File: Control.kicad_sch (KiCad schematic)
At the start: 42 parts, among them U2 LT6108IMS8-1-TRPBF, U3 LM139ADRG4, U5 LT6108IMS8-1-TRPBF

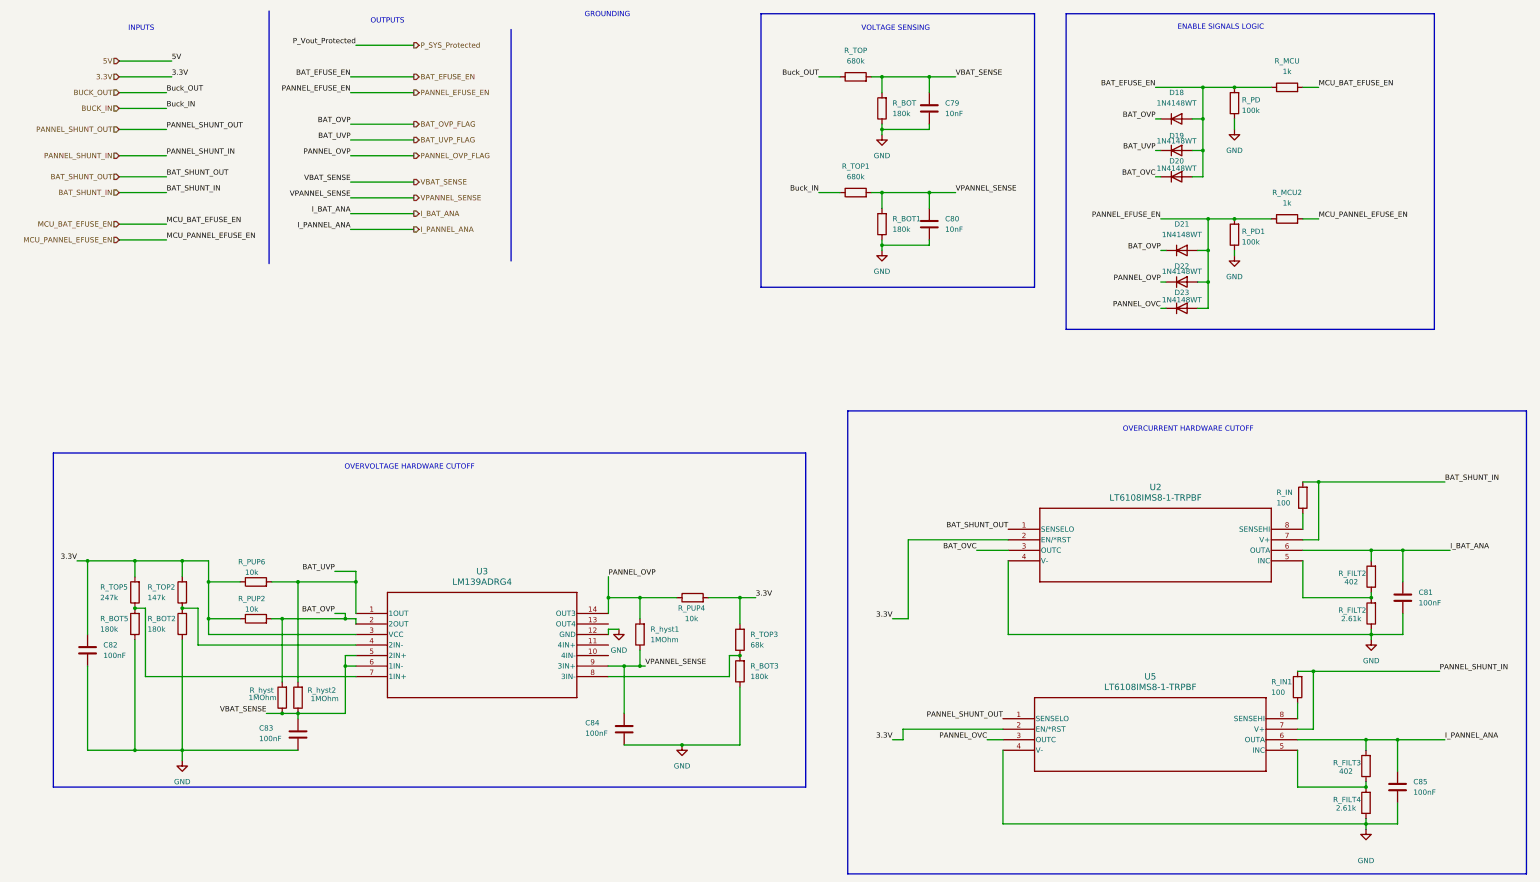
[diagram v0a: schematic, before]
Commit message: Adjusting footprints of components
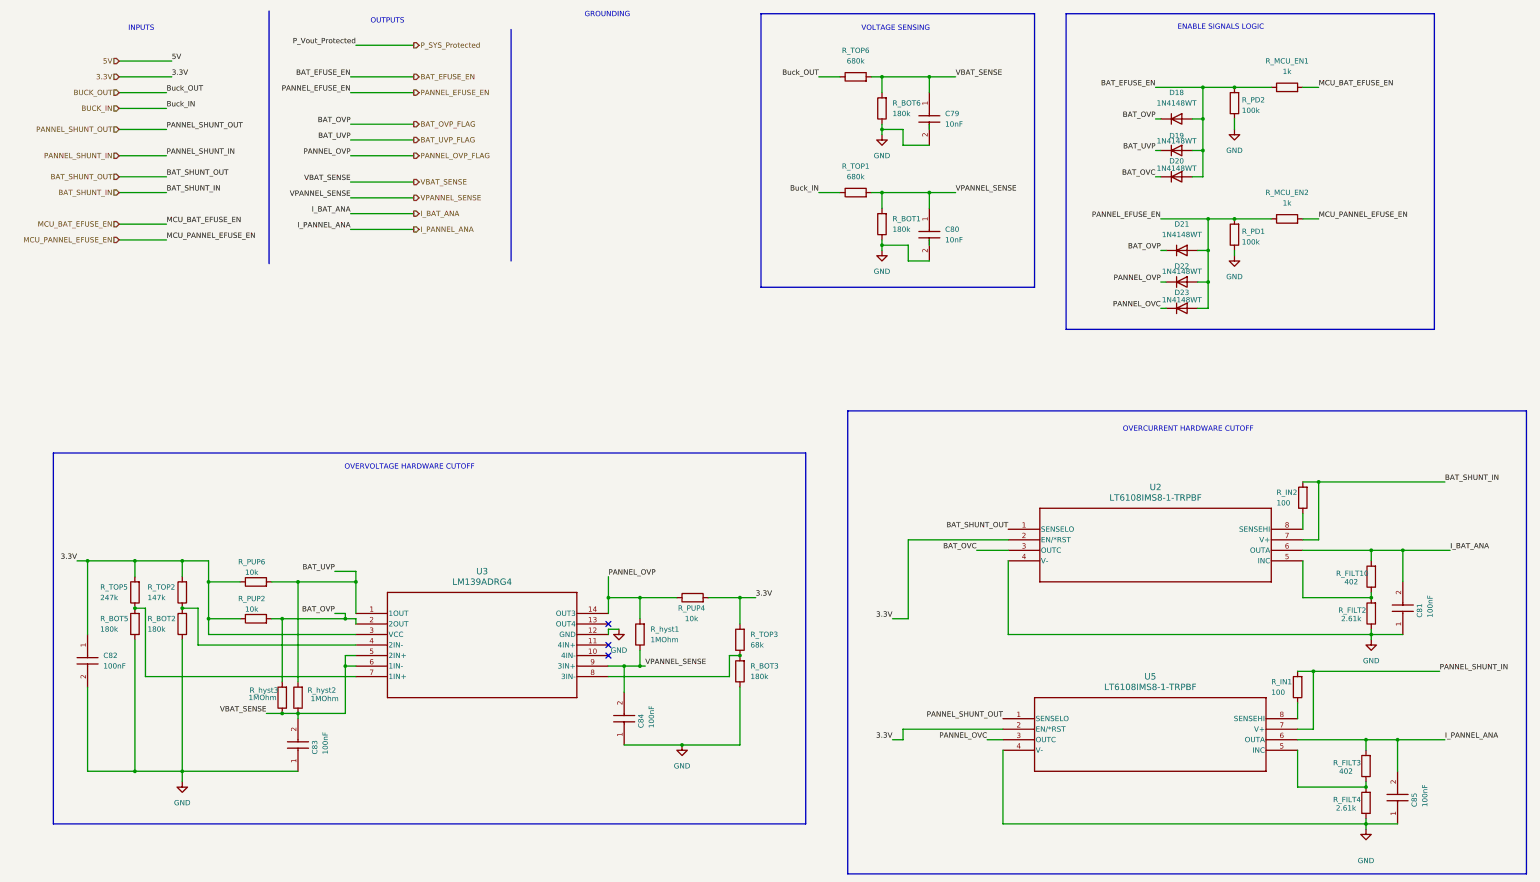
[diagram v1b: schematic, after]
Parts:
- removed C81, C84, C85: 100nF, symbol Device:C
- added C81, C84, C85: 100nF, C0603_Commercial, symbol PULSE_Library:C0603X6S0J104M030BC
- C79, C80: footprint (none) -> CAPC2012X145N; symbol Device:C -> PULSE_Library:C2012X7R1A106M125AC; Height (none) -> 1.45; Manufacturer_Name (none) -> TDK; Manufacturer_Part_Number (none) -> C2012X7R1A106M125AC; Mouser Part Number (none) -> 810-C2012X7R1A106M; Mouser Price/Stock (none) -> https://www.mouser.co.uk/ProductDetail/TDK/C2012X7R1A106M12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
- C82, C83: footprint (none) -> C0603_Commercial; symbol Device:C -> PULSE_Library:C0603X6S0J104M030BC; Height (none) -> 0.33; Manufacturer_Name (none) -> TDK; Manufacturer_Part_Number (none) -> C0603X6S0J104M030BC; Mouser Part Number (none) -> 810-C0603X6S0J104M; Mouser Price/Stock (none) -> https://www.mouser.co.uk/ProductDetail/TDK/C0603X6S0J104M03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
- R_BOT1, R_BOT2, R_BOT3, R_BOT5, R_FILT2, R_FILT3, R_FILT4, R_IN1, R_PD1, R_PUP2, R_PUP4, R_PUP6, R_TOP1, R_TOP2, R_TOP3, R_TOP5, R_hyst1, R_hyst2: footprint (none) -> Resistor_SMD:R_0603_1608Metric
- R_BOT6: renamed from R_BOT; footprint (none) -> Resistor_SMD:R_0603_1608Metric
- R_FILT10: renamed from R_FILT2; footprint (none) -> Resistor_SMD:R_0603_1608Metric
- R_IN2: renamed from R_IN; footprint (none) -> Resistor_SMD:R_0603_1608Metric
- R_MCU_EN1: renamed from R_MCU; footprint (none) -> Resistor_SMD:R_0603_1608Metric
- R_MCU_EN2: renamed from R_MCU2; footprint (none) -> Resistor_SMD:R_0603_1608Metric
- R_PD2: renamed from R_PD; footprint (none) -> Resistor_SMD:R_0603_1608Metric
- R_TOP6: renamed from R_TOP; footprint (none) -> Resistor_SMD:R_0603_1608Metric
- R_hyst3: renamed from R_hyst; footprint (none) -> Resistor_SMD:R_0603_1608Metric
- U2, U5: footprint MSOP-8_MS_LIT -> PULSE_Library:MSOP-8_MS_LIT
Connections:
- net GND: now also C83.1, C81.1, C84.1, C85.1; no longer C83.2
- net I_BAT_ANA: now also C81.2
- net I_PANNEL_ANA: now also C85.2
- net VBAT_SENSE: now also C83.2; no longer C83.1
- net VPANNEL_SENSE: now also C84.2
- no-connect marks 0 -> 3

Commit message: Big final PCU PCB design
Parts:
- added C93: 10nF, PULSE_Library:CAPC2012X145N, symbol PULSE_Library:C2012X7R1A106M125AC
- added R_BOT8: 180k, Resistor_SMD:R_0603_1608Metric, symbol Device:R
- added R_BYPASS2, R_BYPASS3, R_BYPASS4, R_BYPASS5, R_BYPASS6, R_BYPASS7: 0, Resistor_SMD:R_0603_1608Metric, symbol Device:R
- added R_TOP8: 680k, Resistor_SMD:R_0603_1608Metric, symbol Device:R
- added TP10: VBAT_SENSE, TestPoint:TestPoint_Pad_D2.0mm, symbol Connector:TestPoint_Probe
- added TP11: BAT_EFUSE_EN, TestPoint:TestPoint_Pad_D2.0mm, symbol Connector:TestPoint_Probe
- added TP12: PANNEL_EFUSE_EN, TestPoint:TestPoint_Pad_D2.0mm, symbol Connector:TestPoint_Probe
- added TP13: MCU_BAT_EFUSE_EN, TestPoint:TestPoint_Pad_D2.0mm, symbol Connector:TestPoint_Probe
- added TP14: MCU_PANNEL_EFUSE_EN, TestPoint:TestPoint_Pad_D2.0mm, symbol Connector:TestPoint_Probe
- added TP15: BAT_UVP, TestPoint:TestPoint_Pad_D2.0mm, symbol Connector:TestPoint_Probe
- added TP16: BAT_OVP, TestPoint:TestPoint_Pad_D2.0mm, symbol Connector:TestPoint_Probe
- added TP17: PANNEL_OVP, TestPoint:TestPoint_Pad_D2.0mm, symbol Connector:TestPoint_Probe
- added TP18: BAT_SHUNT_OUT, TestPoint:TestPoint_Pad_D2.0mm, symbol Connector:TestPoint_Probe
- added TP19: BAT_SHUNT_IN, TestPoint:TestPoint_Pad_D2.0mm, symbol Connector:TestPoint_Probe
- added TP20: PANNEL_SHUNT_OUT, TestPoint:TestPoint_Pad_D2.0mm, symbol Connector:TestPoint_Probe
- added TP21: PANNEL_SHUNT_IN, TestPoint:TestPoint_Pad_D2.0mm, symbol Connector:TestPoint_Probe
- added TP8: VPANNEL_SENSE, TestPoint:TestPoint_Pad_D2.0mm, symbol Connector:TestPoint_Probe
- added TP9: VCHG_RAIL_SENSE, TestPoint:TestPoint_Pad_D2.0mm, symbol Connector:TestPoint_Probe
- C79, C80: footprint CAPC2012X145N -> PULSE_Library:CAPC2012X145N
- C81, C82, C83, C84, C85: footprint C0603_Commercial -> Capacitor_SMD:C_0603_1608Metric
- U3: footprint D14 -> Package_DIP:CERDIP-14_W7.62mm_SideBrazed_LongPads_Socket
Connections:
- net BAT_EFUSE_EN: now also TP11.1
- net BAT_OVC: now also R_BYPASS4.1; no longer D20.1 (K)
- net BAT_OVP_FLAG: now also R_BYPASS2.1, R_BYPASS5.1, TP16.1; no longer D18.1 (K), D21.1 (K)
- net BAT_SHUNT_IN: now also TP19.1
- net BAT_SHUNT_OUT: now also TP18.1
- net BAT_UVP_FLAG: now also R_BYPASS3.1, TP15.1; no longer D19.1 (K)
- net GND: now also C93.2, R_BOT8.1
- net MCU_BAT_EFUSE_EN: now also TP13.1
- net MCU_PANNEL_EFUSE_EN: now also TP14.1
- net PANNEL_EFUSE_EN: now also TP12.1
- net PANNEL_OVC: now also R_BYPASS7.1; no longer D23.1 (K)
- net PANNEL_OVP_FLAG: now also R_BYPASS6.1, TP17.1; no longer D22.1 (K)
- net PANNEL_SHUNT_IN: now also TP21.1
- net PANNEL_SHUNT_OUT: now also TP20.1
- net VBAT_SENSE: now also C93.1, R_BOT8.2, R_TOP8.2, TP10.1; no longer C79.1, R_BOT6.2, R_TOP6.2
- net VPANNEL_SENSE: now also TP8.1
- new net: D18.1 (K), R_BYPASS2.2
- new net: D19.1 (K), R_BYPASS3.2
- new net: D20.1 (K), R_BYPASS4.2
- new net: D23.1 (K), R_BYPASS7.2
- new net: D22.1 (K), R_BYPASS6.2
- new net: D21.1 (K), R_BYPASS5.2
- new net VBAT: R_TOP8.1
- new net VCHG_RAIL_SENSE: C79.1, R_BOT6.2, R_TOP6.2, TP9.1
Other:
- moved on the sheet: C79, C80, D21, D22, D23, R_BOT1, R_BOT6, R_MCU_EN2, R_PD1, R_TOP1, R_TOP6, U3

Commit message: Modofications asked and BOM
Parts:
- U2, U5: Mouser Part Number (none) -> 584-LT6108AIMS8-1PBF; Mouser link (none) -> https://www.mouser.ch/ProductDetail/Analog-Devices/LT6108AI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
- U3: Mouser Part Number (none) -> 595-LM139DR; Mouser link (none) -> https://www.mouser.ch/ProductDetail/Texas-Instruments/LM139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
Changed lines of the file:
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@@
 			)
 		)
+		(property "Mouser Part Number" "584-LT6108AIMS8-1PBF"
+			(at 254 139.7 0)
+			(effects
+				(font
+					(size 1.27 1.27)
+				)
+				(hide yes)
+			)
+		)
+		(property "Mouser link" "https://www.mouser.ch/ProductDetail/Analog-Devices/LT6108AIMS8-1PBF?qs=hVkxg5c3xu%252Bx53HojhZ%2Faw%3D%3D"
+			(at 254 139.7 0)
+			(effects
+				(font
+					(size 1.27 1.27)
+				)
+				(hide yes)
+			)
+		)
 		(pin "3"
 		)
@@
 			)
 		)
+		(property "Mouser Part Number" "595-LM139DR"
+			(at 99.06 160.02 0)
+			(effects
+				(font
+					(size 1.27 1.27)
+				)
+				(hide yes)
+			)
+		)
+		(property "Mouser link" "https://www.mouser.ch/ProductDetail/Texas-Instruments/LM139DR?qs=q81XD9WTF%252BLzGfVMa%252BrIYQ%3D%3D&utm_id=22436684839&utm_source=google&utm_medium=cpc&utm_marketing_tactic=emeacorp&gad_source=1&gad_campaignid=22433179847&gbraid=0AAAAADn_wf3NeSFef5TwkkK9q0ylaU7DA&gclid=Cj0KCQiAo4TKBhDRARIsAGW29beRf0v6AEFq77btjbKOccqhqNvt5wva_3BCM3JskwQq2kz6-058CTwaAtczEALw_wcB"
+			(at 99.06 160.02 0)
+			(effects
+				(font
+					(size 1.27 1.27)
+				)
+				(hide yes)
+			)
+		)
 		(pin "2"
 		)
@@
 			(at 252.73 185.42 0)
 			(effects
+				(font
+					(size 1.27 1.27)
+				)
+				(hide yes)
+			)
+		)
+		(property "Mouser Part Number" "584-LT6108AIMS8-1PBF"
+			(at 252.73 185.42 0)
+			(effects
+				(font
+					(size 1.27 1.27)
+				)
+				(hide yes)
+			)
+		)
+		(property "Mouser link" "https://www.mouser.ch/ProductDetail/Analog-Devices/LT6108AIMS8-1PBF?qs=hVkxg5c3xu%252Bx53HojhZ%2Faw%3D%3D"
+			(at 252.73 185.42 0)
+			(effects
